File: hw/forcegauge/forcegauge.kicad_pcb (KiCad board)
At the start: 2 copper layers, 68 parts, among them J1 USB_B_Micro, J2 Battery, J3 OLDED_Screen, J4 Conn_01x05, Q1 FDS6892A, Q2 BSS138, Q3 SM2331PSA P-MOSFET, Q4 S8550, Q5 FDS6892A, SW1 SW_Push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

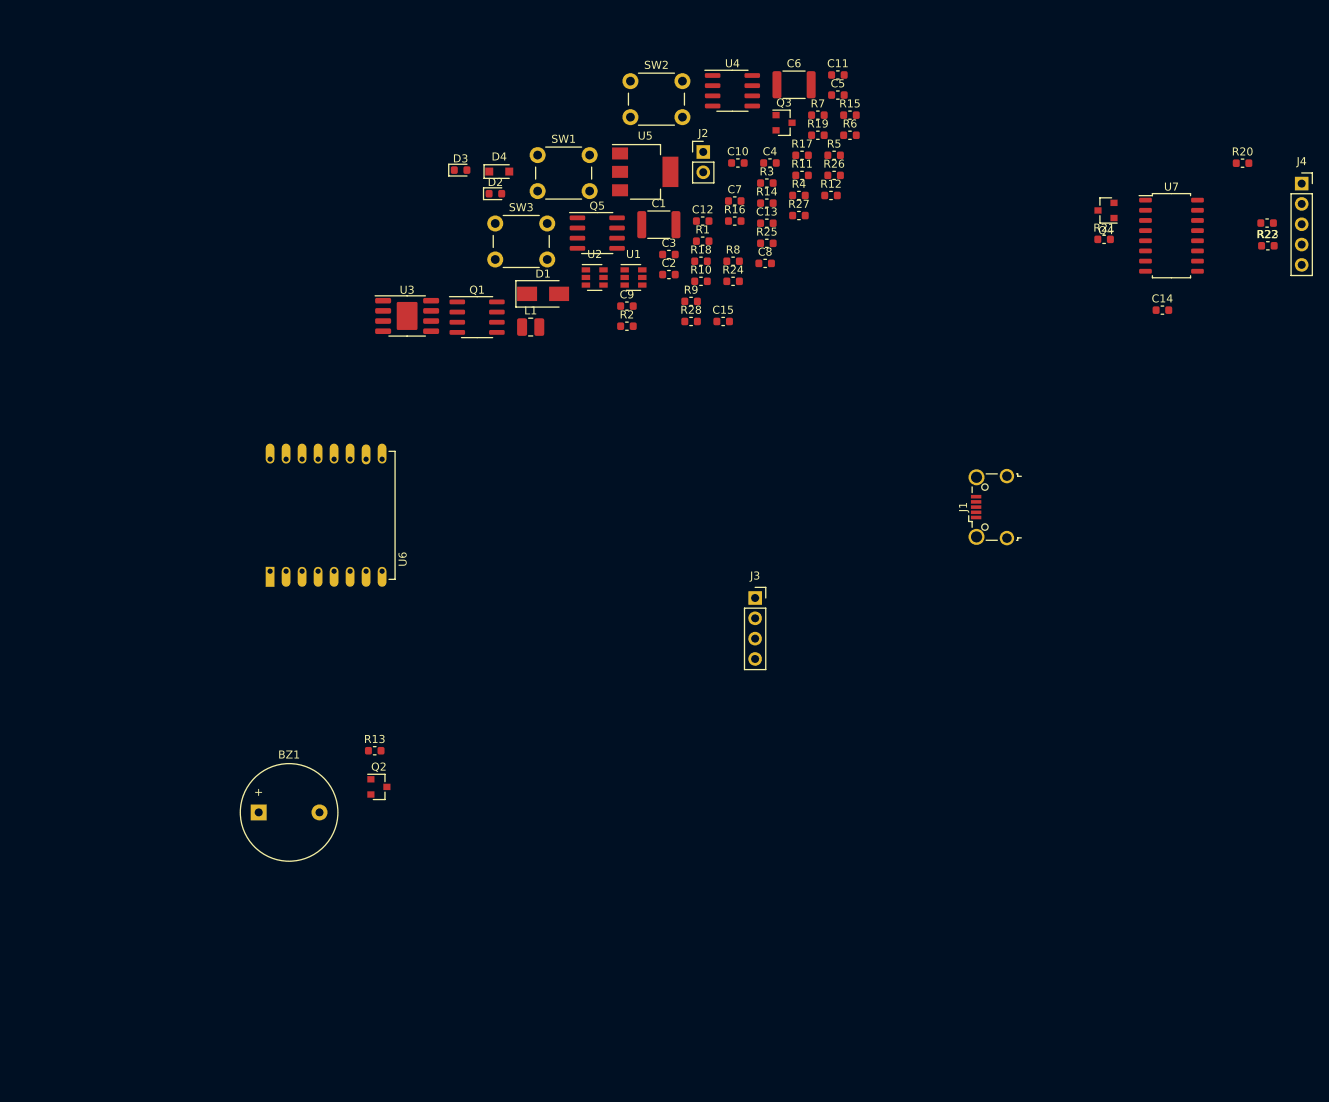
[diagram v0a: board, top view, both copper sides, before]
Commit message: kicad 6, pcb WIP
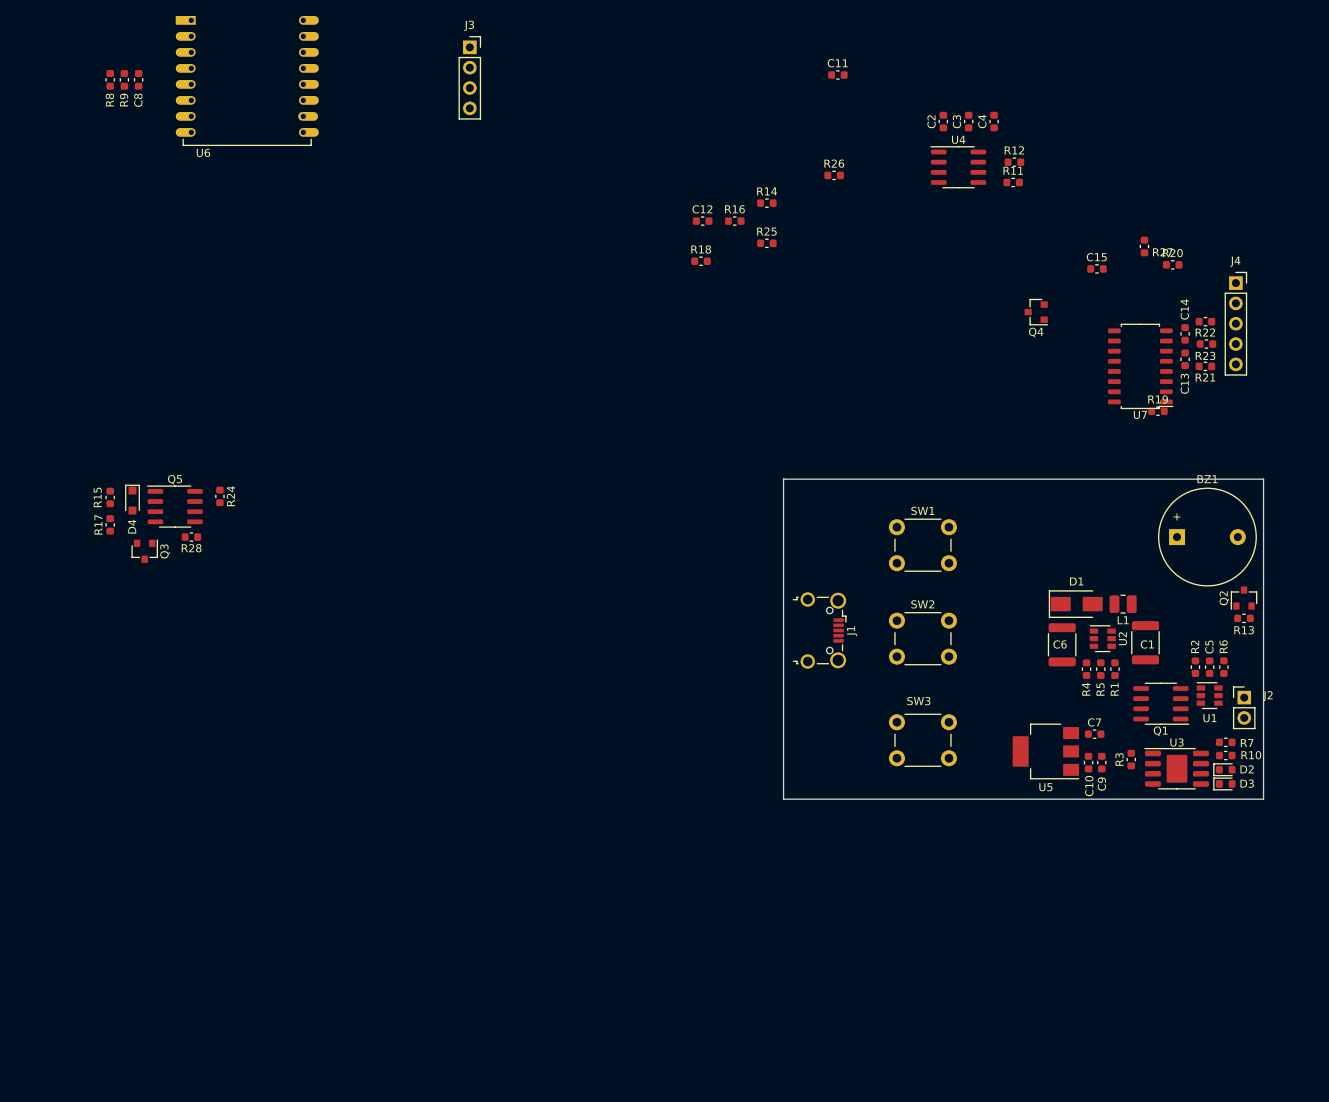
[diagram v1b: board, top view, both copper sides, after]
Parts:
- moved D3 122.6 mm to (208.0, 125.3)
- moved BZ1 119.8 mm to (201.9, 94.5)
- moved D2 116.3 mm to (208.0, 123.6)
- moved U3 111.6 mm to (201.9, 123.4)
- moved Q2 110.7 mm to (210.3, 102.1), turned to 90 degrees
- moved R13 109.9 mm to (210.3, 104.6), turned to 180 degrees
- moved R15 104.1 mm to (68.6, 89.5), turned to -90 degrees
- moved Q1 98.2 mm to (199.9, 115.3), turned to 180 degrees
- moved R17 98.0 mm to (68.6, 93.0), turned to 90 degrees
- moved Q3 96.2 mm to (72.9, 96.3), turned to -90 degrees
- moved J2 96.0 mm to (210.3, 114.6)
- moved R7 93.5 mm to (208.0, 120.1), turned to 180 degrees
- moved U1 89.0 mm to (206.0, 114.3)
- moved R10 88.4 mm to (208.0, 121.8), turned to 180 degrees
- moved U5 88.1 mm to (185.5, 121.3), turned to 180 degrees
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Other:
- board outline added: 60 x 40 mm
- net class Default removed

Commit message: pcb WIP
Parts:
- moved R6 139.2 mm to (74.2, 149.8)
- moved C5 139.2 mm to (72.4, 149.8)
- moved R2 139.2 mm to (70.6, 149.8)
- moved U1 136.8 mm to (75.1, 153.9)
- moved C7 136.6 mm to (59.3, 152.9), turned to 90 degrees
- moved Q1 136.3 mm to (69.3, 154.2)
- moved D2 133.3 mm to (79.9, 160.3)
- moved R10 133.3 mm to (79.9, 158.5)
- moved R7 133.3 mm to (79.9, 156.8)
- moved D3 133.3 mm to (79.9, 162.1)
- moved R3 133.3 mm to (68.1, 159.0)
- moved U3 133.3 mm to (73.8, 160.1)
- moved C9 132.9 mm to (62.9, 152.0), turned to 0 degrees
- moved J2 132.4 mm to (83.2, 151.5)
- moved C10 131.7 mm to (62.9, 153.7), turned to 0 degrees
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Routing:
- net (no net): vias 0 -> 4
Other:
- outline, holes or cut-outs redrawn

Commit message: pcb WIP
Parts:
- moved C5 112.2 mm to (174.9, 103.8), turned to 180 degrees
- moved R3 111.8 mm to (169.1, 111.0), turned to 0 degrees
- moved R2 111.0 mm to (171.7, 103.8), turned to 0 degrees
- moved Q1 110.1 mm to (169.1, 107.4)
- moved R6 110.0 mm to (174.9, 105.4), turned to 0 degrees
- moved U5 109.8 mm to (156.2, 103.3), turned to 90 degrees
- moved U1 109.6 mm to (174.9, 108.3)
- moved U3 108.0 mm to (171.7, 114.4)
- moved C7 107.4 mm to (157.4, 109.0), turned to 180 degrees
- moved R7 106.0 mm to (175.5, 111.0)
- moved R15 105.8 mm to (163.2, 105.2), turned to 180 degrees
- moved D2 105.2 mm to (176.6, 118.7), turned to -90 degrees
- moved D3 104.5 mm to (175.0, 118.7), turned to -90 degrees
- moved R17 103.9 mm to (160.7, 105.9), turned to -90 degrees
- moved R10 103.8 mm to (172.3, 111.0)
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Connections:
- D4 pad 1: GND -> Net-(D4-Pad1)
- J1 pad 4: Net-(J1-Pad4) -> unconnected-(J1-Pad4)
- Q5 pad 1: Net-(Q5-Pad1) -> GND
- Q5 pad 2: GND -> Net-(D4-Pad1)
- Q5 pad 5: Net-(Q5-Pad1) -> GND
- Q5 pad 6: Net-(Q5-Pad1) -> GND
- R15 pad 1: GND -> Net-(D4-Pad1)
- R28 pad 1: Net-(Q5-Pad1) -> GND
- SW2 pad 1: GND -> Net-(D4-Pad1)
- SW2 pad 2: Net-(Q5-Pad1) -> GND
- U1 pad 1: Net-(U1-Pad1) -> Net-(Q1-Pad4)
- U1 pad 4: Net-(U1-Pad4) -> unconnected-(U1-Pad4)
- U2 pad 6: Net-(U2-Pad6) -> unconnected-(U2-Pad6)
- U4 pad 4: Net-(U4-Pad4) -> unconnected-(U4-Pad4)
- U7 pad 13: Net-(U7-Pad13) -> unconnected-(U7-Pad13)
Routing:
- added copper zone on F.Cu, net GND
- added copper zone on In1.Cu, net GND
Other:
- copper layers 2 -> 4

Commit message: PCB wip
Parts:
- added C16: 100nF, Capacitor_SMD:C_0603_1608Metric, F.Cu at (167.6, 96.9)
- moved R27 3.47 mm to (165.2, 98.1), turned to 0 degrees
- moved R21 1.85 mm to (160.0, 87.0)
- moved R20 1.75 mm to (161.8, 87.0), turned to 90 degrees
- moved U4 0.86 mm to (140.9, 110.5)
- moved C3 0.67 mm to (141.9, 107.0)
- moved C2 0.67 mm to (138.7, 107.0)
- moved Q2 0.49 mm to (133.7, 108.1)
- moved R13 0.40 mm to (130.3, 107.3)
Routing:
- net DOUT: track 0.00 -> 37.0 mm
- net CLK: track 0.00 -> 35.0 mm
- net BTN_1: track 0.00 -> 32.2 mm
- net BTN_2: track 0.00 -> 27.1 mm
- net PWR_EN: track 0.00 -> 24.3 mm
- net BTN_3: track 0.00 -> 18.7 mm
- net E+: track 0.00 -> 18.3 mm, vias 0 -> 1
- net BUZZER: track 0.00 -> 16.0 mm
- net E-: track 0.00 -> 14.1 mm
- net Net-(C14-Pad2): track 0.00 -> 14.1 mm, vias 0 -> 2
- net VBUS: track 0.00 -> 12.8 mm
- net Net-(R2-Pad1): track 0.00 -> 9.34 mm
- net Net-(D4-Pad1): track 0.00 -> 9.12 mm
- net Net-(C14-Pad1): track 0.00 -> 7.73 mm, vias 0 -> 2
- net Net-(BZ1-Pad2): track 0.00 -> 7.57 mm
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
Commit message: pcb routing finished, todo check
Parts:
- added H1: MountingHole, forcegauge:MountingHole_2mm_OLED, F.Cu at (178.2, 89.0)
- added H2: MountingHole, forcegauge:MountingHole_2mm_OLED, F.Cu at (154.4, 89.0)
- added H3: MountingHole, forcegauge:MountingHole_2mm_OLED, F.Cu at (154.4, 112.3)
- added H4: MountingHole, forcegauge:MountingHole_2mm_OLED, F.Cu at (178.2, 112.3)
- moved R6 5.02 mm to (178.3, 109.1), turned to 180 degrees
- moved C5 4.95 mm to (178.3, 107.4)
- moved D3 4.40 mm to (177.4, 115.1), turned to 0 degrees
- moved R2 3.91 mm to (175.1, 105.7)
- moved D2 2.21 mm to (177.4, 116.7), turned to 0 degrees
- moved D4 0.51 mm to (149.6, 107.2)
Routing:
- net BAT+: track 0.00 -> 113.5 mm, vias 0 -> 3
- net +3V3: track 0.00 -> 101.4 mm, vias 0 -> 5
- net +5V: track 0.00 -> 90.2 mm, vias 0 -> 2
- net VBUS: track 12.8 -> 64.0 mm, vias 0 -> 3
- net SDA: track 0.00 -> 49.9 mm
- net SCL: track 0.00 -> 47.5 mm
- net BTN_2: track 27.1 -> 61.5 mm, vias 0 -> 2
- net TXD: track 0.00 -> 31.6 mm, vias 0 -> 1
- net RXD: track 0.00 -> 29.9 mm, vias 0 -> 1
- net Net-(D4-Pad1): track 9.12 -> 38.3 mm
- net Net-(D4-Pad2): track 0.00 -> 22.3 mm
- net BAT-: track 7.17 -> 28.2 mm, vias 0 -> 1
- net GND: track 0.00 -> 15.6 mm, vias 0 -> 50
- net 5V_EN: track 0.00 -> 9.96 mm, vias 0 -> 2
- net Net-(D3-Pad2): track 0.00 -> 9.18 mm
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- added copper zone on B.Cu, net GND
- removed copper zone on In1.Cu, net GND
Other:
- copper layers 4 -> 2
- rule pad_to_mask_clearance: 0.051 -> 0
- rule solder_mask_min_width: 0.25 -> 0.12
- board text added: "B+"
- board text added: "B-"
- board text added: "Forcegauge© v0.1"
- board text added: "Load Cell"
- board text added: "OLED"
- board text added: "by Beni"

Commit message: pcb v0.1 sent
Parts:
- D2: value LED -> LED RED
- D3: value LED -> LED GREEN
- J4: value Conn_01x05 -> Load Cell
- moved R2 0.78 mm to (174.3, 105.5), turned to 180 degrees
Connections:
- R2 pad 2: BAT- -> GND
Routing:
- net BAT-: track 28.2 -> 28.7 mm
- net GND: vias 50 -> 51
